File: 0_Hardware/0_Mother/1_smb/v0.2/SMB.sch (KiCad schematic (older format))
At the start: 50 parts, among them IC1 MAX485, IC101 ATMEGA1284-A, IC2 DS2482-100S, J101 RJ45, J102 RTS_RESET, J103 ICSP, J104 SERIAL_REV, P101 I2C_CONN, P102 CONN_10X2, P103 CONN_5, P105 CONN_5, P107 CONN_3, P108 CONN_5, P109 CONN_3, P110 CONN_3, P112 CONN_3, P2 CONN_3, SW101 SKQGAKE010, X101 20MHz

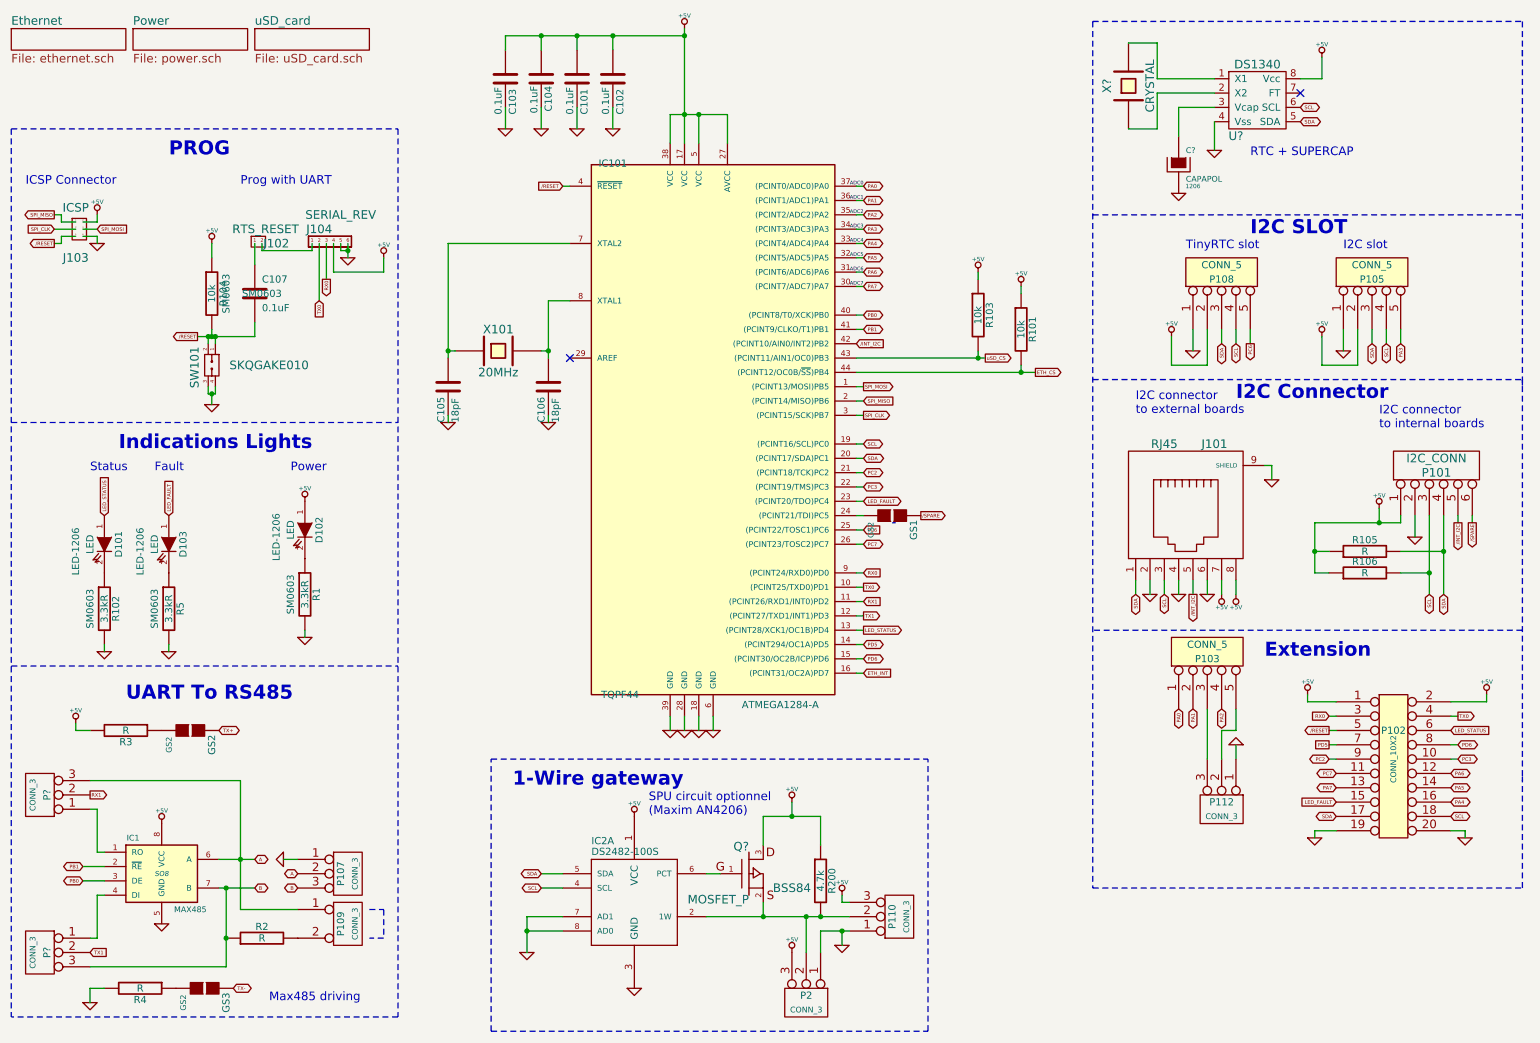
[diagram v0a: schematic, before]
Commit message: mise à jour smb v0.2 (schéma, package, routage). Todo: vérifier les packages des nouveaux composants
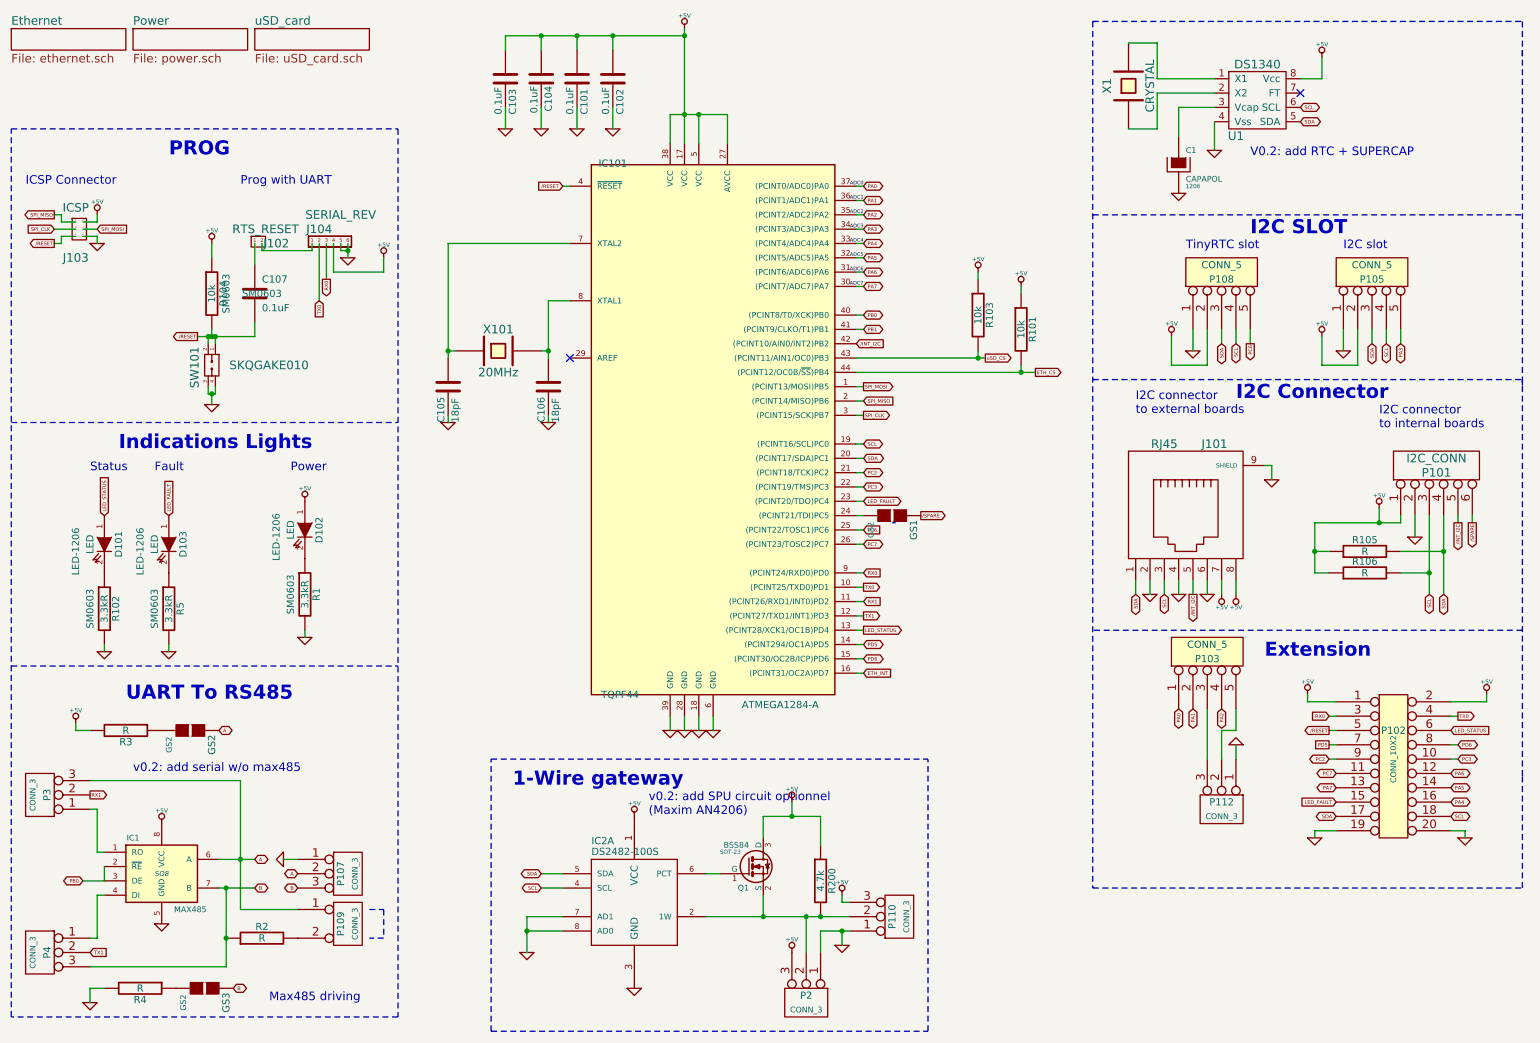
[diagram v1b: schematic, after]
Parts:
- removed Q?: MOSFET_P, symbol MOSFET_P
- added Q1: BSS84, SOT-23, symbol BSS138
- gave numbers to parts that had none: 5
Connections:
- net TX+ is gone; now on net A: GS2.1 (G1)
- net TX- is gone; now on net B: GS3.1 (G1)
- net +5V: now also Q1.3 (D)
- net PB0: now also IC1.2 (~RE~)
- net PB1: no longer IC1.2 (~RE~)
- net at IC2.2 (1W), P110.2 (PM), P2.2 (PM)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: now also Q1.2 (S)
- net at IC2.6 (PCT): now also Q1.1 (G)
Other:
- note added: "V0.2: add RTC + SUPERCAP"
- note added: "v0.2: add SPU circuit optionnel\n(Maxim AN4206)"
- note added: "v0.2: add serial w/o max485"
- note removed: "RTC + SUPERCAP"
- note removed: "SPU circuit optionnel\n(Maxim AN4206)"

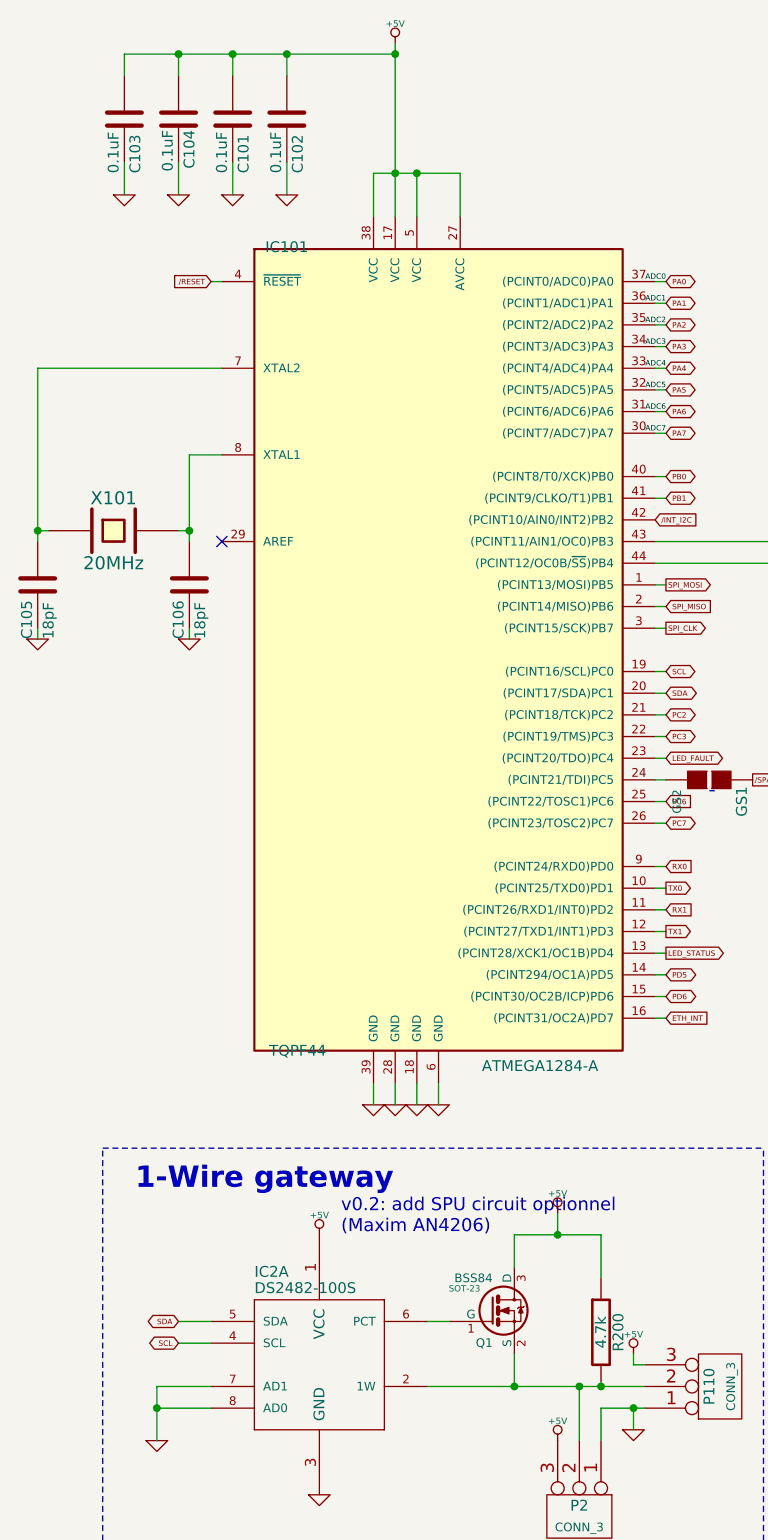
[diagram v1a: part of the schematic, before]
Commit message: SMB v0.2: remplacement composant mosfet par type P
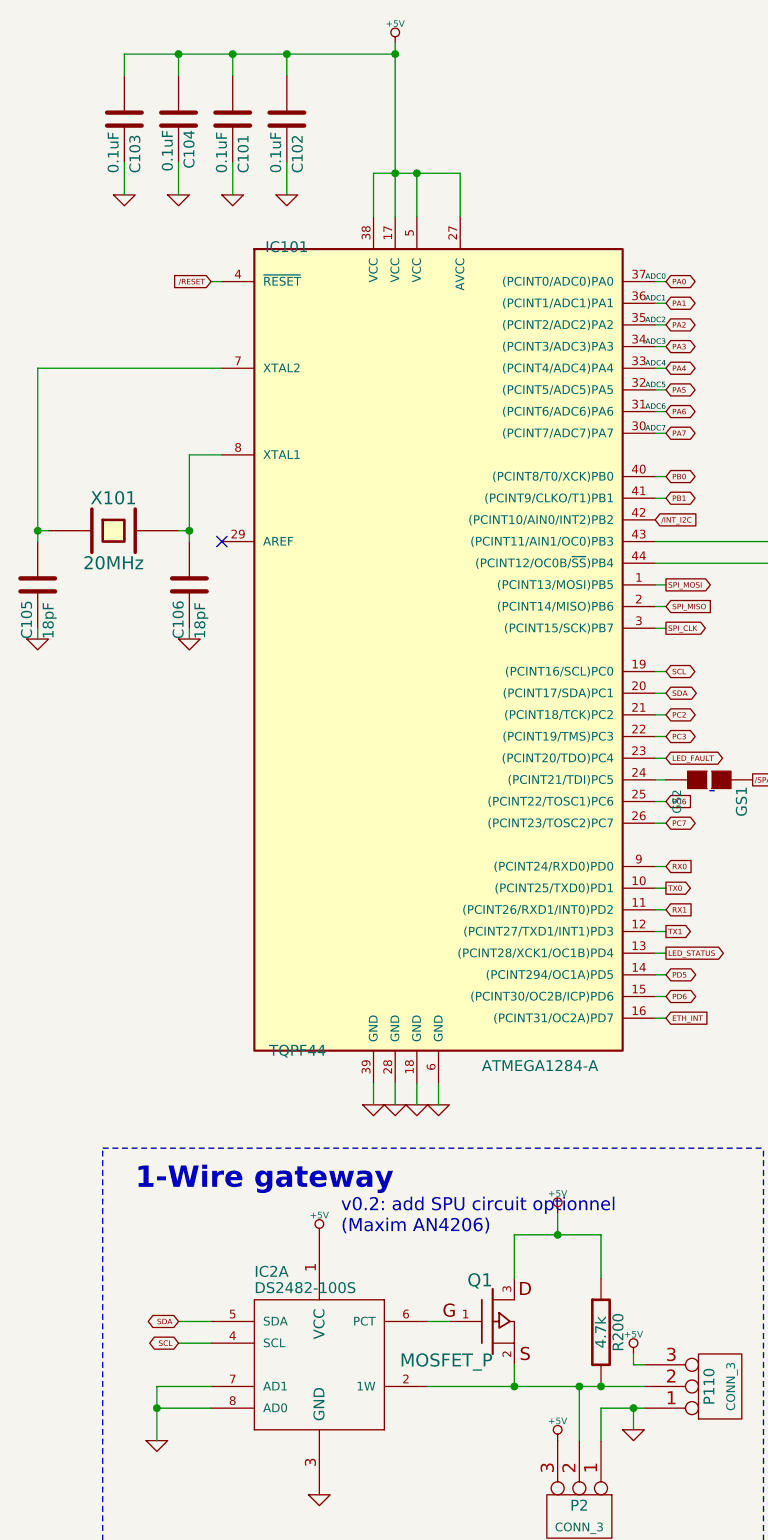
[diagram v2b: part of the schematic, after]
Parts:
- removed Q1: BSS84, SOT-23, symbol BSS138
- added Q1: MOSFET_P, ~, symbol MOSFET_P
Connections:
- net +5V: now also Q1.3
- net at IC2.2 (1W), P110.2 (PM), P2.2 (PM)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: now also Q1.2
- net at IC2.6 (PCT): now also Q1.1
